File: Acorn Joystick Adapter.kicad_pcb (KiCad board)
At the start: 2 copper layers, 64.1 x 38.7 mm, 17 parts, among them J1 BBC Micro, J2 Atari #1, J3 Atari #2, Q1 BC337, Q2 BC337, Q3 BC337

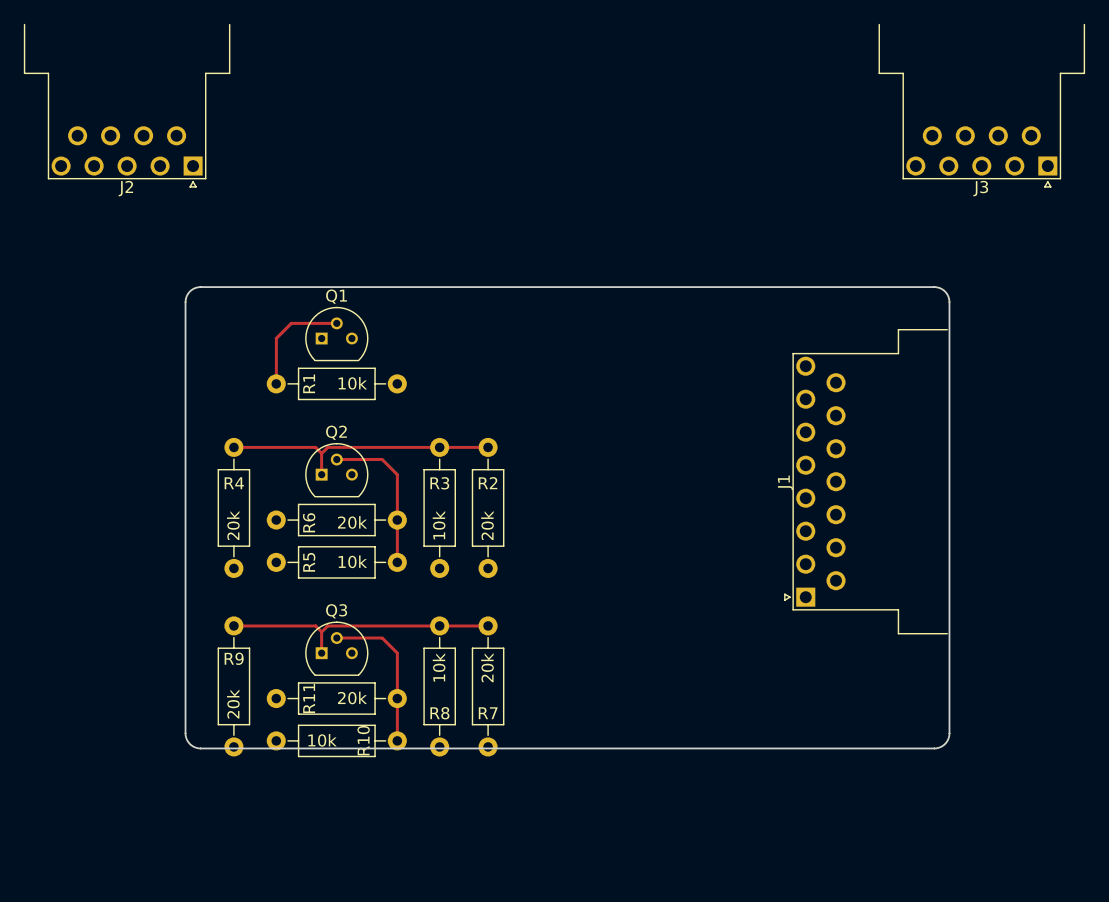
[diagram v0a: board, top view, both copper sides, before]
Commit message: Changed transistor footprint and pcb layout
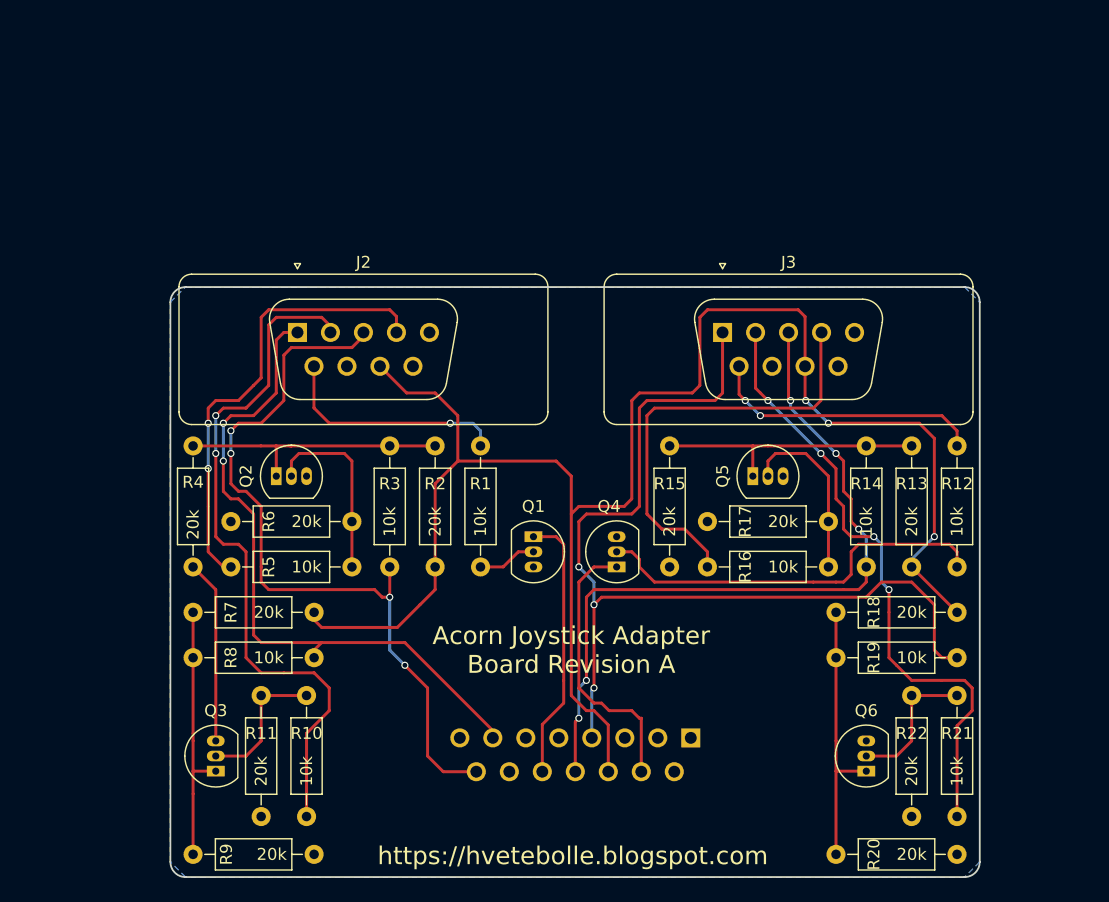
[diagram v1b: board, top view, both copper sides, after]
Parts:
- added Q4: BC337, TO_SOT_Packages_THT:TO-92_Inline_Narrow_Oval, F.Cu at (130.2, 116.2)
- added Q5: BC337, TO_SOT_Packages_THT:TO-92_Inline_Narrow_Oval, F.Cu at (141.6, 108.6)
- added Q6: BC337, TO_SOT_Packages_THT:TO-92_Inline_Narrow_Oval, F.Cu at (151.1, 133.3)
- added R12: 10k, Resistors_THT:R_Axial_DIN0207_L6.3mm_D2.5mm_P10.16mm_Horizontal, F.Cu at (158.8, 106.0)
- added R13: 20k, Resistors_THT:R_Axial_DIN0207_L6.3mm_D2.5mm_P10.16mm_Horizontal, F.Cu at (154.9, 116.2)
- added R14: 10k, Resistors_THT:R_Axial_DIN0207_L6.3mm_D2.5mm_P10.16mm_Horizontal, F.Cu at (151.1, 106.0)
- added R15: 20k, Resistors_THT:R_Axial_DIN0207_L6.3mm_D2.5mm_P10.16mm_Horizontal, F.Cu at (134.6, 106.0)
- added R16: 10k, Resistors_THT:R_Axial_DIN0207_L6.3mm_D2.5mm_P10.16mm_Horizontal, F.Cu at (148.0, 116.2)
- added R17: 20k, Resistors_THT:R_Axial_DIN0207_L6.3mm_D2.5mm_P10.16mm_Horizontal, F.Cu at (148.0, 112.4)
- added R18: 20k, Resistors_THT:R_Axial_DIN0207_L6.3mm_D2.5mm_P10.16mm_Horizontal, F.Cu at (158.8, 120.0)
- added R19: 10k, Resistors_THT:R_Axial_DIN0207_L6.3mm_D2.5mm_P10.16mm_Horizontal, F.Cu at (148.6, 123.8)
- added R20: 20k, Resistors_THT:R_Axial_DIN0207_L6.3mm_D2.5mm_P10.16mm_Horizontal, F.Cu at (148.6, 140.3)
- added R21: 10k, Resistors_THT:R_Axial_DIN0207_L6.3mm_D2.5mm_P10.16mm_Horizontal, F.Cu at (158.8, 127.0)
- added R22: 20k, Resistors_THT:R_Axial_DIN0207_L6.3mm_D2.5mm_P10.16mm_Horizontal, F.Cu at (154.9, 127.0)
- J1: value BBC Micro -> Acorn Computer; footprint Connectors_DSub:DSUB-15_Male_Horizontal_Pitch2.77x2.54mm_EdgePinOffset9.40mm -> Connectors_DSub:DSUB-15_Male_Vertical_Pitch2.77x2.84mm; moved to B.Cu
- J2, J3: footprint Connectors_DSub:DSUB-9_Male_Horizontal_Pitch2.77x2.54mm_EdgePinOffset9.40mm -> Connectors_DSub:DSUB-9_Male_Vertical_Pitch2.77x2.84mm
- Q1, Q2, Q3: footprint TO_SOT_Packages_THT:TO-92_Molded_Narrow -> TO_SOT_Packages_THT:TO-92_Inline_Narrow_Oval
- moved J3 30.7 mm to (139.1, 96.5), turned to 0 degrees
- moved Q1 24.3 mm to (123.2, 113.7), turned to 270 degrees
- moved R8 20.9 mm to (94.6, 123.8), turned to 0 degrees
- moved R9 19.5 mm to (94.6, 140.3), turned to 0 degrees
- moved R7 18.5 mm to (104.8, 120.0), turned to 180 degrees
- moved J2 16.5 mm to (103.4, 96.5), turned to 0 degrees
- moved J1 15.3 mm to (136.4, 130.6), turned to 180 degrees
- moved Q3 13.3 mm to (96.5, 133.3), turned to 90 degrees
- moved R11 11.4 mm to (100.3, 127.0), turned to 270 degrees
- moved R1 8.71 mm to (118.7, 106.0), turned to 270 degrees
- moved R10 8.52 mm to (104.1, 127.0), turned to 270 degrees
- moved R2 4.45 mm to (114.9, 116.2)
- moved R3 4.19 mm to (111.1, 106.0)
- moved R5 3.83 mm to (108.0, 116.2)
- moved Q2 3.81 mm to (101.6, 108.6)
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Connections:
- net A_DOWN renamed A1_DOWN
- net A_FIRE renamed A1_FIRE
- net A_LEFT renamed A1_LEFT
- net A_RIGHT renamed A1_RIGHT
- net A_UP renamed A1_UP
- J1 pad 10: (no net) -> B_PB1
- J1 pad 11: A_GND -> VREF
- J1 pad 12: (no net) -> A2_LEFT
- J1 pad 4: (no net) -> A2_UP
- J2 pad 8: A_GND -> VREF
- J3 pad 1: (no net) -> A2_UP
- J3 pad 2: (no net) -> A2_DOWN
- J3 pad 3: (no net) -> A2_LEFT
- J3 pad 4: (no net) -> A2_RIGHT
- J3 pad 6: (no net) -> A2_FIRE
- J3 pad 8: (no net) -> VREF
- R2 pad 1: A_GND -> VREF
- R7 pad 1: A_GND -> VREF
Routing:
- net VREF: track 0.00 -> 143.8 mm, vias 0 -> 3
- net A2_UP: track 0.00 -> 81.3 mm, vias 0 -> 3
- net A1_LEFT: track 0.00 -> 64.2 mm, vias 0 -> 4
- net A2_LEFT: track 0.00 -> 62.7 mm, vias 0 -> 5
- net A1_DOWN: track 0.00 -> 58.6 mm, vias 0 -> 2
- net A1_UP: track 0.00 -> 56.9 mm, vias 0 -> 2
- net A2_DOWN: track 0.00 -> 52.4 mm, vias 0 -> 4
- net A1_RIGHT: track 0.00 -> 38.3 mm, vias 0 -> 2
- net A2_RIGHT: track 0.00 -> 36.8 mm
- net Net-(Q4-Pad2): track 0.00 -> 34.0 mm
- net B_PB1: track 0.00 -> 23.4 mm
- net A2_FIRE: track 0.00 -> 23.2 mm, vias 0 -> 2
- net Net-(Q6-Pad1): track 0.00 -> 22.9 mm
- net Net-(Q5-Pad1): track 0.00 -> 22.9 mm
- net B_PB0: track 0.00 -> 22.6 mm
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- added copper zone on B.Cu, net GNDA
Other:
- board size 64.1 x 38.7 mm -> 67.9 x 49.5 mm
- board text added: "Acorn Joystick Adapter Board Revision A"
- board text added: "https://hvetebolle.blogspot.com"

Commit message: Resized board to match plastic enclosure height
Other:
- board size 67.9 x 49.5 mm -> 67.9 x 52.1 mm
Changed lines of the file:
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@@
     (links 58)
     (no_connects 0)
-    (area 92.634999 92.634999 160.730001 142.315001)
+    (area 92.634999 90.094999 160.730001 142.315001)
     (thickness 1.6)
-    (drawings 11)
+    (drawings 14)
     (tracks 324)
     (zones 0)
@@
     (descr "9-pin D-Sub connector, straight/vertical, THT-mount, male, pitch 2.77x2.84mm, distance of mounting holes 25mm, see https://disti-assets.s3.amazonaws.com/tonar/files/datasheets/16730.pdf")
     (tags "9-pin D-Sub connector straight vertical THT male pitch 2.77x2.84mm mounting holes distance 25mm")
-    (fp_text reference J2 (at 5.54 -5.89) (layer F.SilkS)
+    (fp_text reference J2 (at 0.127 -7.62) (layer F.SilkS)
       (effects (font (size 1 1) (thickness 0.15)))
     )
@@
     (descr "9-pin D-Sub connector, straight/vertical, THT-mount, male, pitch 2.77x2.84mm, distance of mounting holes 25mm, see https://disti-assets.s3.amazonaws.com/tonar/files/datasheets/16730.pdf")
     (tags "9-pin D-Sub connector straight vertical THT male pitch 2.77x2.84mm mounting holes distance 25mm")
-    (fp_text reference J3 (at 5.54 -5.89) (layer F.SilkS)
+    (fp_text reference J3 (at 0 -7.62) (layer F.SilkS)
       (effects (font (size 1 1) (thickness 0.15)))
     )
@@
     )
   )
+  (gr_text https://hvetebolle.blogspot.com (at 126.365 140.335) (layer B.SilkS)
+    (effects (font (size 1.5 1.5) (thickness 0.3)) (justify mirror))
+  )
+  (gr_line (start 160.655 91.44) (end 160.655 93.98) (angle 90) (layer Edge.Cuts) (width 0.15))
+  (gr_line (start 93.98 90.17) (end 159.385 90.17) (angle 90) (layer Edge.Cuts) (width 0.15))
+  (gr_line (start 92.71 91.44) (end 92.71 93.98) (angle 90) (layer Edge.Cuts) (width 0.15))
   (gr_text "Acorn Joystick Adapter\nBoard Revision A" (at 126.365 121.92) (layer B.SilkS)
     (effects (font (size 1.5 1.5) (thickness 0.3)) (justify mirror))
   )
-  (gr_text https://hvetebolle.blogspot.com (at 126.492 140.462) (layer F.SilkS)
+  (gr_text https://hvetebolle.blogspot.com (at 126.365 140.335) (layer F.SilkS)
     (effects (font (size 1.5 1.5) (thickness 0.3)))
   )
@@
     (effects (font (size 1.5 1.5) (thickness 0.3)))
   )
-  (gr_arc (start 159.385 93.98) (end 159.385 92.71) (angle 90) (layer Edge.Cuts) (width 0.15))
-  (gr_line (start 159.385 92.71) (end 93.98 92.71) (angle 90) (layer Edge.Cuts) (width 0.15))
+  (gr_arc (start 159.385 91.44) (end 159.385 90.17) (angle 90) (layer Edge.Cuts) (width 0.15))
   (gr_line (start 160.655 140.97) (end 160.655 93.98) (angle 90) (layer Edge.Cuts) (width 0.15))
   (gr_line (start 93.98 142.24) (end 159.385 142.24) (angle 90) (layer Edge.Cuts) (width 0.15))
   (gr_arc (start 159.385 140.97) (end 160.655 140.97) (angle 90) (layer Edge.Cuts) (width 0.15))
   (gr_line (start 92.71 140.97) (end 92.71 93.98) (angle 90) (layer Edge.Cuts) (width 0.15))
-  (gr_arc (start 93.98 93.98) (end 92.71 93.98) (angle 90) (layer Edge.Cuts) (width 0.15))
+  (gr_arc (start 93.98 91.44) (end 92.71 91.44) (angle 90) (layer Edge.Cuts) (width 0.15))
   (gr_arc (start 93.98 140.97) (end 93.98 142.24) (angle 90) (layer Edge.Cuts) (width 0.15))
   (segment (start 96.52 130.81) (end 96.52 118.11) (width 0.25) (layer F.Cu) (net 1))
